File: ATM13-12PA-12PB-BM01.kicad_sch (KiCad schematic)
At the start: 25 parts

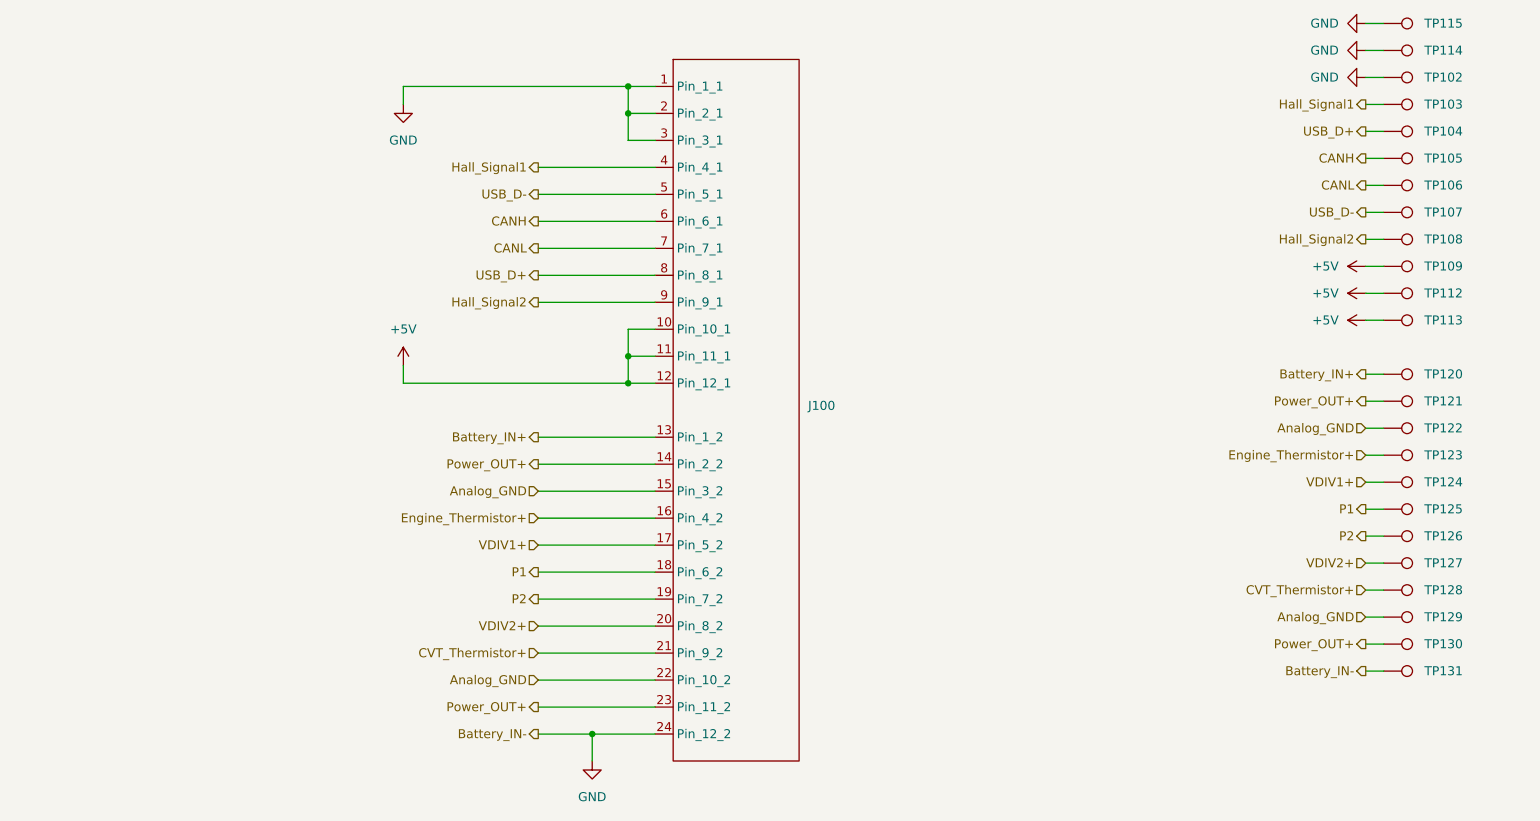
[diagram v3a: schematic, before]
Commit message: removed a VDIV input and changed it to a thermistor input. Re-ran fabrication output
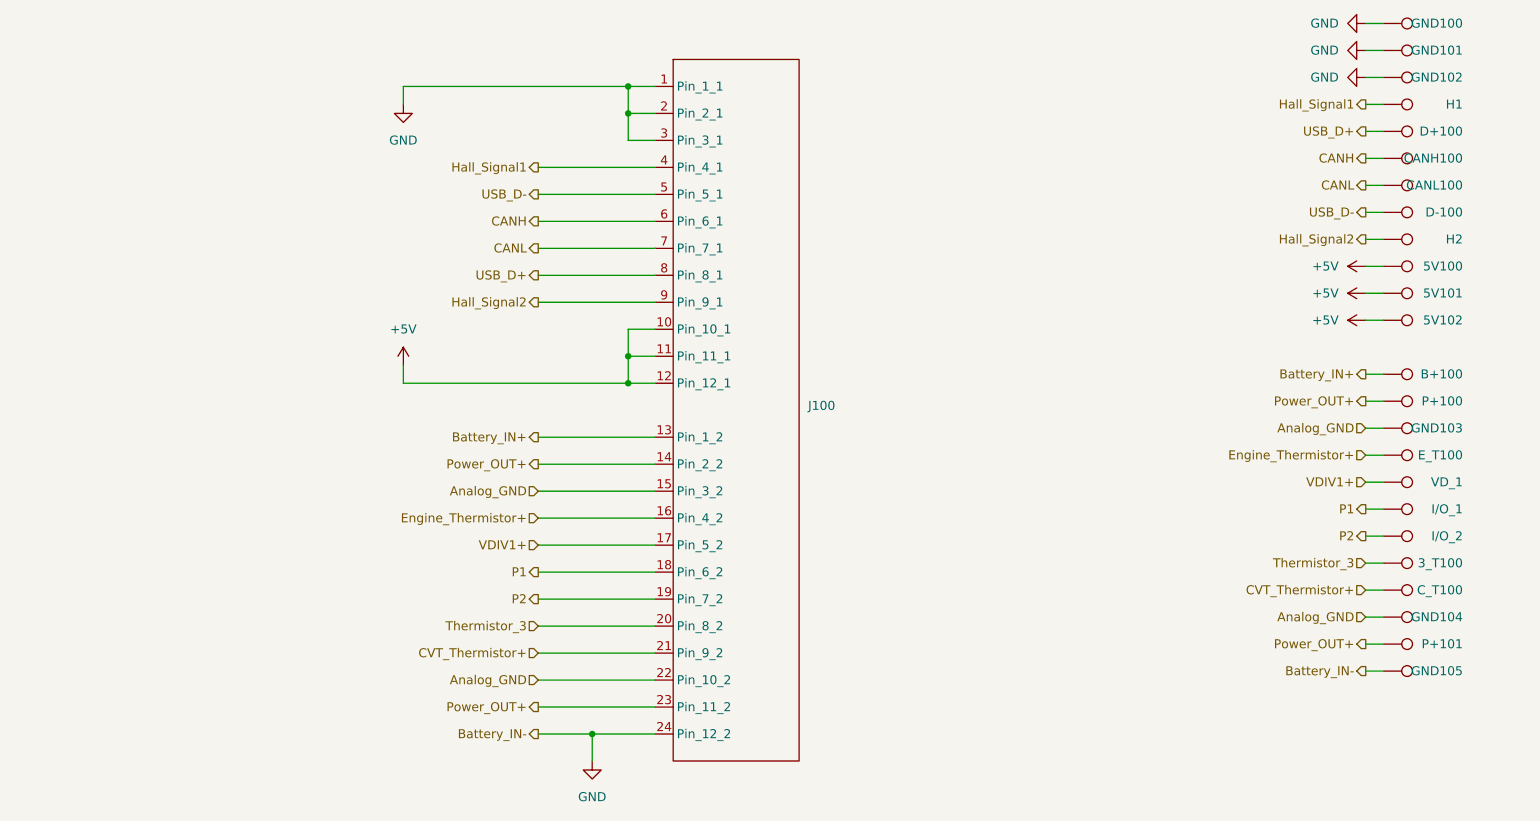
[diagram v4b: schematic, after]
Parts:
- renumbered TP127 to 3_T100, TP109 to 5V100, TP112 to 5V101, TP113 to 5V102, TP120 to B+100, TP105 to CANH100, TP106 to CANL100, TP128 to C_T100, TP104 to D+100, TP107 to D-100, TP123 to E_T100, TP115 to GND100, TP114 to GND101, TP102 to GND102, TP122 to GND103, TP129 to GND104, TP131 to GND105, TP103 to H1, TP108 to H2, TP125 to I/O_1, TP126 to I/O_2, TP121 to P+100, TP130 to P+101, TP124 to VD_1
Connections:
- net VDIV2+ renamed Thermistor_3
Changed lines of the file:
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@@
-		)
-	)
-	(hierarchical_label "VDIV2+"
-		(shape input)
-		(at 224.79 119.38 180)
-		(effects
-			(font
-				(size 1.27 1.27)
-			)
-			(justify right)
 		)
 	)
@@
 		)
 	)
+	(hierarchical_label "Thermistor_3"
+		(shape input)
+		(at 224.79 119.38 180)
+		(effects
+			(font
+				(size 1.27 1.27)
+			)
+			(justify right)
+		)
+	)
 	(hierarchical_label "Hall_Signal2"
 		(shape output)
@@
 		)
 	)
-	(hierarchical_label "VDIV2+"
+	(hierarchical_label "Thermistor_3"
 		(shape input)
 		(at 107.95 128.27 180)
@@
 		(on_board yes)
 		(dnp no)
-		(property "Reference" "TP122"
+		(property "Reference" "GND103"
 			(at 238.506 100.33 90)
 			(effects
@@
 			(project "TeensyDAQ_REV0"
 				(path "/11737956-c422-45b5-a9a0-ee63a853502c/36af939c-a039-4370-9390-49414daba697"
-					(reference "TP122")
+					(reference "GND103")
 					(unit 1)
 				)
@@
 		(on_board yes)
 		(dnp no)
-		(property "Reference" "TP123"
+		(property "Reference" "E_T100"
 			(at 238.506 104.14 90)
 			(effects
@@
 			(project "TeensyDAQ_REV0"
 				(path "/11737956-c422-45b5-a9a0-ee63a853502c/36af939c-a039-4370-9390-49414daba697"
-					(reference "TP123")
+					(reference "E_T100")
 					(unit 1)
 				)
@@
 		(on_board yes)
 		(dnp no)
-		(property "Reference" "TP105"
+		(property "Reference" "CANH100"
 			(at 238.506 62.23 90)
 			(effects
@@
 			(project "TeensyDAQ_REV0"
 				(path "/11737956-c422-45b5-a9a0-ee63a853502c/36af939c-a039-4370-9390-49414daba697"
-					(reference "TP105")
+					(reference "CANH100")
 					(unit 1)
 				)
@@
 		(on_board yes)
 		(dnp no)
-		(property "Reference" "TP125"
+		(property "Reference" "I/O_1"
 			(at 238.506 111.76 90)
 			(effects
@@
 			(project "TeensyDAQ_REV0"
 				(path "/11737956-c422-45b5-a9a0-ee63a853502c/36af939c-a039-4370-9390-49414daba697"
-					(reference "TP125")
+					(reference "I/O_1")
 					(unit 1)
 				)
@@
 		(on_board yes)
 		(dnp no)
-		(property "Reference" "TP120"
+		(property "Reference" "B+100"
 			(at 238.506 92.71 90)
 			(effects
@@
 			(project "TeensyDAQ_REV0"
 				(path "/11737956-c422-45b5-a9a0-ee63a853502c/36af939c-a039-4370-9390-49414daba697"
-					(reference "TP120")
+					(reference "B+100")
 					(unit 1)
 				)
@@
 		(on_board yes)
 		(dnp no)
-		(property "Reference" "TP108"
+		(property "Reference" "H2"
 			(at 238.506 73.66 90)
 			(effects
@@
 			(project "TeensyDAQ_REV0"
 				(path "/11737956-c422-45b5-a9a0-ee63a853502c/36af939c-a039-4370-9390-49414daba697"
-					(reference "TP108")
+					(reference "H2")
 					(unit 1)
 				)
@@
 		(on_board yes)
 		(dnp no)
-		(property "Reference" "TP102"
+		(property "Reference" "GND102"
 			(at 238.506 50.8 90)
 			(effects
@@
 			(project "TeensyDAQ_REV0"
 				(path "/11737956-c422-45b5-a9a0-ee63a853502c/36af939c-a039-4370-9390-49414daba697"
-					(reference "TP102")
+					(reference "GND102")
 					(unit 1)
 				)
@@
 		(on_board yes)
 		(dnp no)
-		(property "Reference" "TP113"
+		(property "Reference" "5V102"
 			(at 238.506 85.09 90)
 			(effects
@@
 			(project "TeensyDAQ_REV0"
 				(path "/11737956-c422-45b5-a9a0-ee63a853502c/36af939c-a039-4370-9390-49414daba697"
-					(reference "TP113")
+					(reference "5V102")
 					(unit 1)
 				)
@@
 		(on_board yes)
 		(dnp no)
-		(property "Reference" "TP130"
+		(property "Reference" "P+101"
 			(at 238.506 130.81 90)
 			(effects
@@
 			(project "TeensyDAQ_REV0"
 				(path "/11737956-c422-45b5-a9a0-ee63a853502c/36af939c-a039-4370-9390-49414daba697"
-					(reference "TP130")
+					(reference "P+101")
 					(unit 1)
 				)
@@
 		(on_board yes)
 		(dnp no)
-		(property "Reference" "TP115"
+		(property "Reference" "GND100"
 			(at 238.506 43.18 90)
 			(effects
@@
 			(project "TeensyDAQ_REV0"
 				(path "/11737956-c422-45b5-a9a0-ee63a853502c/36af939c-a039-4370-9390-49414daba697"
-					(reference "TP115")
+					(reference "GND100")
 					(unit 1)
 				)
@@
 		(on_board yes)
 		(dnp no)
-		(property "Reference" "TP128"
+		(property "Reference" "C_T100"
 			(at 238.506 123.19 90)
 			(effects
@@
 			(project "TeensyDAQ_REV0"
 				(path "/11737956-c422-45b5-a9a0-ee63a853502c/36af939c-a039-4370-9390-49414daba697"
-					(reference "TP128")
+					(reference "C_T100")
 					(unit 1)
 				)
@@
 		(on_board yes)
 		(dnp no)
-		(property "Reference" "TP126"
+		(property "Reference" "I/O_2"
 			(at 238.506 115.57 90)
 			(effects
@@
 			(project "TeensyDAQ_REV0"
 				(path "/11737956-c422-45b5-a9a0-ee63a853502c/36af939c-a039-4370-9390-49414daba697"
-					(reference "TP126")
+					(reference "I/O_2")
 					(unit 1)
 				)
@@
 		(on_board yes)
 		(dnp no)
-		(property "Reference" "TP114"
+		(property "Reference" "GND101"
 			(at 238.506 46.99 90)
 			(effects
@@
 			(project "TeensyDAQ_REV0"
 				(path "/11737956-c422-45b5-a9a0-ee63a853502c/36af939c-a039-4370-9390-49414daba697"
-					(reference "TP114")
+					(reference "GND101")
 					(unit 1)
 				)
@@
 		(on_board yes)
 		(dnp no)
-		(property "Reference" "TP103"
+		(property "Reference" "H1"
 			(at 238.506 54.61 90)
 			(effects
@@
 			(project "TeensyDAQ_REV0"
 				(path "/11737956-c422-45b5-a9a0-ee63a853502c/36af939c-a039-4370-9390-49414daba697"
-					(reference "TP103")
+					(reference "H1")
 					(unit 1)
 				)
@@
 		(on_board yes)
 		(dnp no)
-		(property "Reference" "TP109"
+		(property "Reference" "5V100"
 			(at 238.506 77.47 90)
 			(effects
@@
 			(project "TeensyDAQ_REV0"
 				(path "/11737956-c422-45b5-a9a0-ee63a853502c/36af939c-a039-4370-9390-49414daba697"
-					(reference "TP109")
+					(reference "5V100")
 					(unit 1)
 				)
@@
 		(on_board yes)
 		(dnp no)
-		(property "Reference" "TP112"
+		(property "Reference" "5V101"
 			(at 238.506 81.28 90)
 			(effects
@@
 			(project "TeensyDAQ_REV0"
 				(path "/11737956-c422-45b5-a9a0-ee63a853502c/36af939c-a039-4370-9390-49414daba697"
-					(reference "TP112")
+					(reference "5V101")
 					(unit 1)
 				)
@@
 		(on_board yes)
 		(dnp no)
-		(property "Reference" "TP124"
+		(property "Reference" "VD_1"
 			(at 238.506 107.95 90)
 			(effects
@@
 			(project "TeensyDAQ_REV0"
 				(path "/11737956-c422-45b5-a9a0-ee63a853502c/36af939c-a039-4370-9390-49414daba697"
-					(reference "TP124")
+					(reference "VD_1")
 					(unit 1)
 				)
@@
 		(on_board yes)
 		(dnp no)
-		(property "Reference" "TP121"
+		(property "Reference" "P+100"
 			(at 238.506 96.52 90)
 			(effects
@@
 			(project "TeensyDAQ_REV0"
 				(path "/11737956-c422-45b5-a9a0-ee63a853502c/36af939c-a039-4370-9390-49414daba697"
-					(reference "TP121")
+					(reference "P+100")
 					(unit 1)
 				)
@@
 		(on_board yes)
 		(dnp no)
-		(property "Reference" "TP131"
+		(property "Reference" "GND105"
 			(at 238.506 134.62 90)
 			(effects
@@
 			(project "TeensyDAQ_REV0"
 				(path "/11737956-c422-45b5-a9a0-ee63a853502c/36af939c-a039-4370-9390-49414daba697"
-					(reference "TP131")
+					(reference "GND105")
 					(unit 1)
 				)
@@
 		(on_board yes)
 		(dnp no)
-		(property "Reference" "TP127"
+		(property "Reference" "3_T100"
 			(at 238.506 119.38 90)
 			(effects
@@
 			(project "TeensyDAQ_REV0"
 				(path "/11737956-c422-45b5-a9a0-ee63a853502c/36af939c-a039-4370-9390-49414daba697"
-					(reference "TP127")
+					(reference "3_T100")
 					(unit 1)
 				)
@@
 		(on_board yes)
 		(dnp no)
-		(property "Reference" "TP129"
+		(property "Reference" "GND104"
 			(at 238.506 127 90)
 			(effects
@@
 			(project "TeensyDAQ_REV0"
 				(path "/11737956-c422-45b5-a9a0-ee63a853502c/36af939c-a039-4370-9390-49414daba697"
-					(reference "TP129")
+					(reference "GND104")
 					(unit 1)
 				)
@@
 		(on_board yes)
 		(dnp no)
-		(property "Reference" "TP106"
+		(property "Reference" "CANL100"
 			(at 238.506 66.04 90)
 			(effects
@@
 			(project "TeensyDAQ_REV0"
 				(path "/11737956-c422-45b5-a9a0-ee63a853502c/36af939c-a039-4370-9390-49414daba697"
-					(reference "TP106")
+					(reference "CANL100")
 					(unit 1)
 				)
@@
 		(on_board yes)
 		(dnp no)
-		(property "Reference" "TP107"
+		(property "Reference" "D-100"
 			(at 238.506 69.85 90)
 			(effects
@@
 			(project "TeensyDAQ_REV0"
 				(path "/11737956-c422-45b5-a9a0-ee63a853502c/36af939c-a039-4370-9390-49414daba697"
-					(reference "TP107")
+					(reference "D-100")
 					(unit 1)
 				)
@@
 		(on_board yes)
 		(dnp no)
-		(property "Reference" "TP104"
+		(property "Reference" "D+100"
 			(at 238.506 58.42 90)
 			(effects
@@
 			(project "TeensyDAQ_REV0"
 				(path "/11737956-c422-45b5-a9a0-ee63a853502c/36af939c-a039-4370-9390-49414daba697"
-					(reference "TP104")
-					(unit 1)
-				)
+					(reference "D+100")
+					(unit 1)
+				)

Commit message: added TVS diodes to external pins for protection. Ran fabrication output. Ran iBOM generation. All part links can be seen in the iBOM. Download and open to see this
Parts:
- removed 3_T100, C_T100, D+100, D-100, E_T100, H1, H2, I/O_1, I/O_2, VD_1: TestPoint, TestPoint:TestPoint_Pad_D1.0mm, symbol Connector:TestPoint
- added D104, D105, D106, D107, D108, D109: SMAJ5.0A, Diode_SMD:D_SMA, symbol Diode:SMAJ5.0A
- J100: DIGIKEY LINK (none) -> https://www.digikey.com/en/products/detail/amphenol-sine-sy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
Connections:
- net CANH: now also D107.1 (A1)
- net CANL: now also D106.1 (A1)
- net GND: now also D104.2 (A2), D105.2 (A2), D106.2 (A2), D107.2 (A2), D108.2 (A2), D109.2 (A2)
- net Hall_Signal1: now also D109.1 (A1)
- net Hall_Signal2: now also D104.1 (A1)
- net USB_D+: now also D105.1 (A1)
- net USB_D-: now also D108.1 (A1)
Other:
- moved on the sheet: 5V100, 5V101, 5V102, B+100, CANH100, CANL100, GND100, GND101, GND102, GND103, GND104, GND105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
